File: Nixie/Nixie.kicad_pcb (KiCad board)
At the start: 2 copper layers, 132.3 x 78.5 mm, 41 parts, among them J1 Conn_01x05_Male, J2 USB_B_Micro, Q1 BC847, Q2 BC847, SW1 SW_Push, U1 K155ID1, U2 ESP-12E, U3 74HC595, U4 K155ID1, U5 K155ID1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

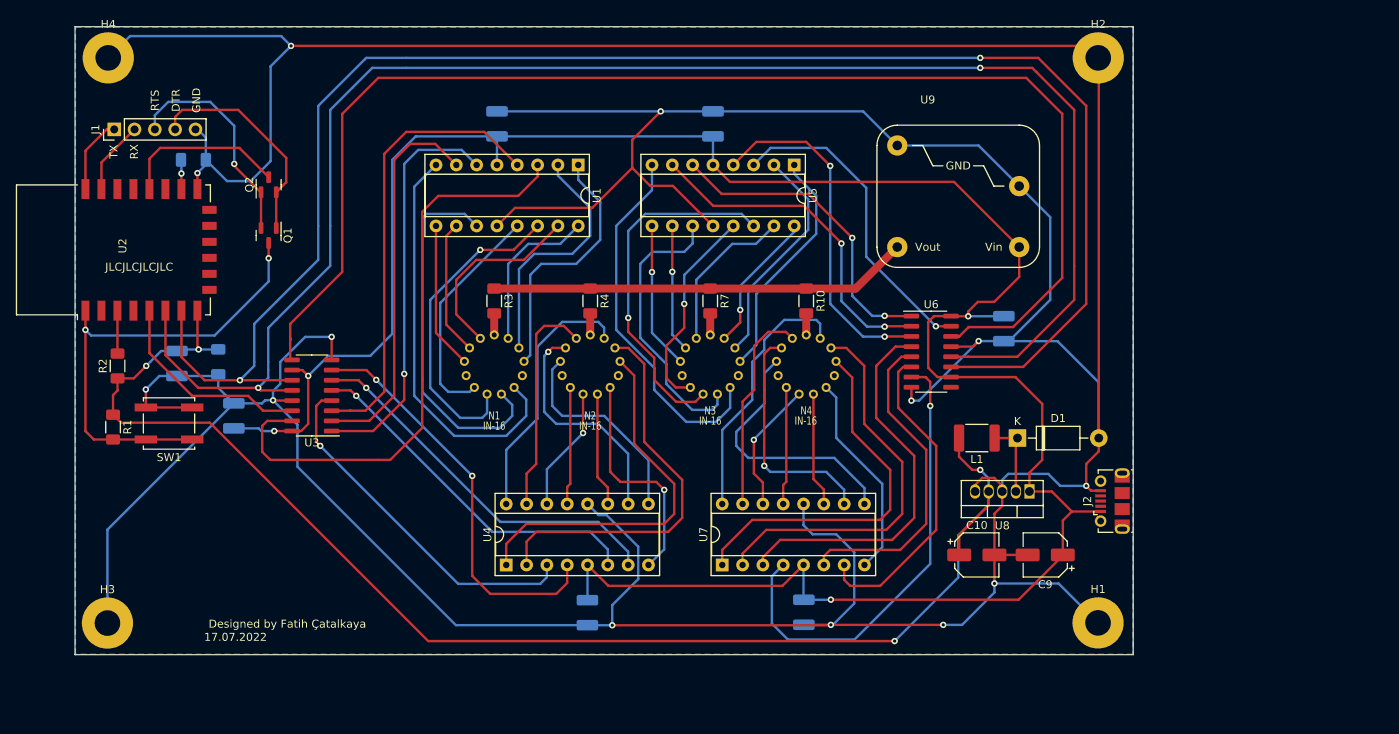
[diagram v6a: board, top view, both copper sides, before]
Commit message: Platine neu gezeichnet mit gmit genauen Maßen
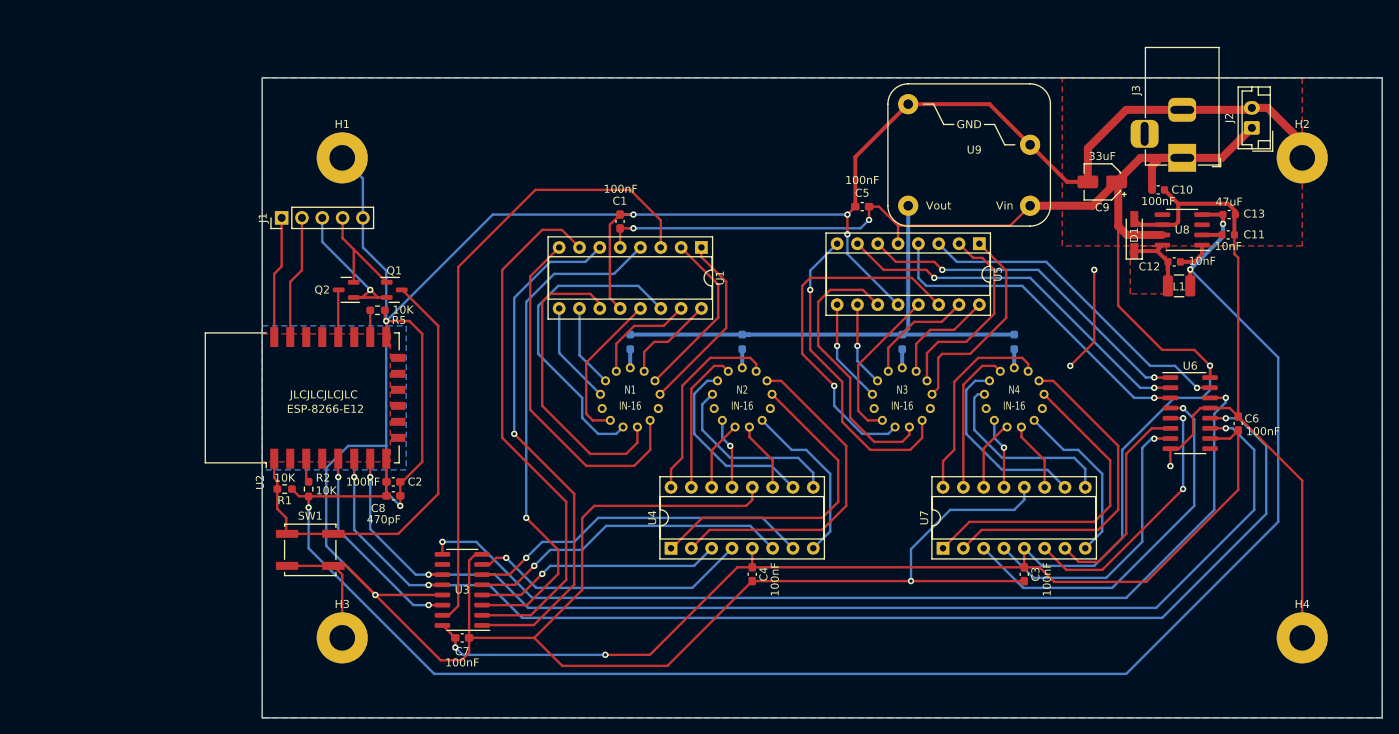
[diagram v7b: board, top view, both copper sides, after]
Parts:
- added C11: 10nF, Capacitor_SMD:C_0603_1608Metric, F.Cu at (200.7, 79.6)
- added C12: 10nF, Capacitor_SMD:C_0603_1608Metric, F.Cu at (194.0, 83.0)
- added C13: 47uF, Capacitor_SMD:C_0603_1608Metric, F.Cu at (200.9, 77.1)
- added J3: Barrel_Jack, Connector_BarrelJack:BarrelJack_Horizontal, F.Cu at (195.0, 70.0)
- C1, C2, C3, C4, C5, C6, C7: value 0.1uF -> 100nF; footprint Capacitor_SMD:C_1210_3225Metric_Pad1.33x2.70mm_HandSolder -> Capacitor_SMD:C_0603_1608Metric_Pad1.08x0.95mm_HandSolder; moved to F.Cu
- C10: value 330uF -> 100nF; footprint Capacitor_SMD:CP_Elec_5x3 -> Capacitor_SMD:C_0603_1608Metric
- C8: footprint Capacitor_SMD:C_1206_3216Metric_Pad1.33x1.80mm_HandSolder -> Capacitor_SMD:C_0603_1608Metric_Pad1.08x0.95mm_HandSolder; moved to F.Cu
- C9: value 330uF -> 33uF; footprint Capacitor_SMD:CP_Elec_5x3 -> Capacitor_SMD:CP_Elec_4x4.5
- D1: value 1N5819 -> SS14FL 1A 40V; footprint Diode_THT:D_DO-41_SOD81_P10.16mm_Horizontal -> diode:D_SMA
- J2: value USB_B_Micro -> Conn_01x02; footprint Connector_USB:USB_Micro-B_Molex-105017-0001 -> Connector_JST:JST_EH_B2B-EH-A_1x02_P2.50mm_Vertical
- L1: value 330uH -> 82uH; footprint Inductor_SMD:L_1812_4532Metric_Pad1.30x3.40mm_HandSolder -> Inductor_SMD:L_1210_3225Metric
- R1, R2: footprint Resistor_SMD:R_1206_3216Metric_Pad1.30x1.75mm_HandSolder -> Resistor_SMD:R_0603_1608Metric_Pad0.98x0.95mm_HandSolder
- R10, R3, R4, R7: footprint Resistor_SMD:R_1206_3216Metric_Pad1.30x1.75mm_HandSolder -> Resistor_SMD:R_0603_1608Metric_Pad0.98x0.95mm_HandSolder; moved to B.Cu
- R5: footprint Resistor_SMD:R_1206_3216Metric_Pad1.30x1.75mm_HandSolder -> Resistor_SMD:R_0603_1608Metric_Pad0.98x0.95mm_HandSolder; moved to F.Cu
- U8: value LM2575-3.3BT -> LM2671M-3.3; footprint Package_TO_SOT_THT:TO-220-5_Vertical -> Package_SO:SOIC-8_3.9x4.9mm_P1.27mm
- moved H4 165.9 mm to (210.0, 130.0)
- moved H1 110.9 mm to (90.0, 70.0)
- moved C3 100.8 mm to (175.2, 122.0), turned to -90 degrees
- moved C5 61.3 mm to (155.0, 76.1), turned to 180 degrees
- moved C4 56.5 mm to (141.2, 122.0), turned to -90 degrees
- moved C10 51.0 mm to (192.0, 74.0)
- moved J2 49.8 mm to (203.7, 66.2)
- moved C9 47.2 mm to (185.0, 73.0)
- moved C7 42.8 mm to (105.0, 130.0), turned to 0 degrees
- moved U8 37.9 mm to (195.0, 79.0)
- moved U6 33.3 mm to (196.0, 101.9)
- moved L1 31.6 mm to (194.6, 86.0), turned to 0 degrees
- moved C6 31.6 mm to (202.0, 103.2), turned to 90 degrees
- moved C2 30.8 mm to (96.4, 110.5), turned to 0 degrees
- moved U3 30.7 mm to (105.0, 124.0)
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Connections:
- C10 pad 1: +3.3V -> +5V
- D1 pad 1: Net-(D1-Pad1) -> /V_{SW}
- J2 pad 2: unconnected-(J2-Pad2) -> GND
- L1 pad 1: Net-(D1-Pad1) -> /V_{SW}
- U8 pad 1: +5V -> Net-(C12-Pad1)
- U8 pad 2: Net-(D1-Pad1) -> /SS
- U8 pad 3: GND -> unconnected-(U8-Pad3)
- U8 pad 5: GND -> +5V
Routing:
- net GND: track 672.6 -> 581.5 mm, vias 13 -> 10
- net SR_CLK: track 205.1 -> 144.3 mm, vias 2 -> 3
- net RCLK: track 201.1 -> 151.5 mm, vias 2 -> 3
- net Net-(U3-Pad9): track 165.0 -> 122.1 mm, vias 0 -> 2
- net +3.3V: track 175.0 -> 208.3 mm, vias 4 -> 3
- net Net-(U6-Pad7): track 57.8 -> 36.4 mm
- net +5V: track 287.8 -> 307.2 mm, vias 4 -> 5
- net Net-(U1-Pad7): track 48.3 -> 67.1 mm
- net Net-(U3-Pad7): track 51.2 -> 35.2 mm, vias 2 -> 1
- net Net-(U1-Pad6): track 50.7 -> 65.9 mm
- net GPIO0: track 20.8 -> 5.93 mm
- net Net-(U3-Pad4): track 44.8 -> 31.1 mm
- net Net-(U6-Pad6): track 40.2 -> 26.7 mm
- net /DTR: track 27.6 -> 14.4 mm
- net 170V: track 52.5 -> 65.3 mm
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- added copper zone on F.Cu, net /RTS
- added copper zone on F.Cu, net /V_{SW}
- added copper zone on F.Cu, net GND
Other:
- board size 132.3 x 78.5 mm -> 140 x 80 mm
- board text added: "10K"
- board text added: "ESP-8266-E12"
- board text removed: "17.07.2022"
- board text removed: "DTR"
- board text removed: "Designed by Fatih Çatalkaya"
- board text removed: "GND"
- board text removed: "RTS"
- board text removed: "RX"
- board text removed: "TX"

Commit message: Small adjustments
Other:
- board text added: "DTR"
- board text added: "Designed by Fatih Çatalkaya 22. Juli 2022"
- board text added: "GND"
- board text added: "RTS"
- board text added: "RX"
- board text added: "TX"
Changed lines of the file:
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@@
     (property "Sheetname" "")
     (attr through_hole)
-    (fp_text reference "J1" (at 0 -2.33 90) (layer "F.SilkS")
+    (fp_text reference "J1" (at 0 12.875 90) (layer "F.SilkS")
       (effects (font (size 1 1) (thickness 0.15)))
     )
@@
   )
   (gr_rect (start 80 60) (end 220 140) (layer "Edge.Cuts") (width 0.1) (fill none))
+  (gr_text "TX" (at 82.5 74.55 90) (layer "F.SilkS")
+    (effects (font (size 1 1) (thickness 0.15)))
+  )
+  (gr_text "RTS" (at 87.5 81 90) (layer "F.SilkS")
+    (effects (font (size 1 1) (thickness 0.15)))
+  )
   (gr_text "10K" (at 82.8 110) (layer "F.SilkS")
     (effects (font (size 1 1) (thickness 0.15)))
   )
+  (gr_text "DTR" (at 90.05 81 90) (layer "F.SilkS")
+    (effects (font (size 1 1) (thickness 0.15)))
+  )
+  (gr_text "RX" (at 85 74.6 90) (layer "F.SilkS")
+    (effects (font (size 1 1) (thickness 0.15)))
+  )
+  (gr_text "GND" (at 92.6 81 90) (layer "F.SilkS")
+    (effects (font (size 1 1) (thickness 0.15)))
+  )
   (gr_text "10K" (at 88 111.6) (layer "F.SilkS")
     (effects (font (size 1 1) (thickness 0.15)))
   )
+  (gr_text "Designed by Fatih Çatalkaya\n22. Juli 2022" (at 114.75 63.375) (layer "F.SilkS")
+    (effects (font (size 1 1) (thickness 0.15)))
+  )
